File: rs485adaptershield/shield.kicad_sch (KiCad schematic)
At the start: 25 parts, among them J2 XT60, J3 RACK OUT 2mm, J4 RACK OUT 2.54mm, U2 Analog_1, U3 Analog_2, U4 ESP32-S3, U6 Digital_1, U7 Digital_2

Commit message: more work
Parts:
- removed C4, C6: 100n, Capacitor_SMD:C_0402_1005Metric, symbol Device:C
- removed J1, J5: (no value), Connector_USB:USB_C_Receptacle_GCT_USB4110, symbol Connector:USB_C_Receptacle_USB2.0_16P
- removed R14, R15, R16, R9: 5.1k, Capacitor_SMD:C_0402_1005Metric, symbol Device:R
- added C12: 100n, Capacitor_SMD:C_0402_1005Metric, symbol Device:C
- added J6: (no value), Connector_USB:USB_C_Receptacle_GCT_USB4110, symbol Connector:USB_C_Receptacle_USB2.0_16P
- added R19, R20: 5.1k, Capacitor_SMD:C_0402_1005Metric, symbol Device:R
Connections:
- net GND: now also C12.2, J6.A1 (GND), J6.A12 (GND), J6.B1 (GND), J6.B12 (GND), R19.2, R20.2
- net +3.3V: now reaches U2.4 (+3V3)
- new net: J6.A4 (VBUS), J6.A9 (VBUS), J6.B4 (VBUS), J6.B9 (VBUS)
- new net: C12.1, J6.SH (SHIELD)
- new net DC+: J6.A6 (D+), J6.B6 (D+)
- new net DC-: J6.A7 (D-), J6.B7 (D-)
- new net USB_CC1C: J6.A5 (CC1), R19.1
- new net USB_CC2C: J6.B5 (CC2), R20.1
- no-connect marks 4 -> 3
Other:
- sheet I&V Sense ports: added none; removed SCL, SDA
- note removed: "1A MAX Silkscreen"
- moved on the sheet: D1, D5, F1, J3, J4, R1, R11, U2, U4, U6, U7

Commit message: more progress
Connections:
- net VIN is gone; now on net VBATT: R1.2
- net +5V: now reaches U2.5 (+5V)
- net VBATT: now reaches U2.6 (GND)
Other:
- sheet RS485 TxRx ports: added none; removed A+, B-, DE, DI, RO, ¬RE
- note added: "Go and relabel all signals with line voltage"
- note added: "Use the dual mos package from power elec to control the usb rst and power supply enable"
- note added: "all the i/o is 5V!"
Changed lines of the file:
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@@
 	(generator_version "10.0")
 	(paper "A4")
+	(text "all the i/o is 5V!\n"
+		(exclude_from_sim no)
+		(at 130.302 105.41 0)
+		(effects
+			(font
+				(size 2.54 2.54)
+				(thickness 0.254)
+				(bold yes)
+			)
+		)
+	)
+	(text "Go and relabel all signals with line voltage\n"
+		(exclude_from_sim no)
+		(at 119.126 112.522 0)
+		(effects
+			(font
+				(size 2.54 2.54)
+				(thickness 0.254)
+				(bold yes)
+			)
+		)
+	)
 	(text "check flipping\n"
 		(exclude_from_sim no)
@@
 		)
 	)
+	(text "Use the dual mos package from power elec to control the usb rst and power supply enable"
+		(exclude_from_sim no)
+		(at 113.03 121.92 0)
+		(effects
+			(font
+				(size 2.54 2.54)
+				(thickness 0.254)
+				(bold yes)
+			)
+		)
+	)
 	(text "check flipping\n"
 		(exclude_from_sim no)
@@
 	)
 	(no_connect
-		(at 184.15 58.42)
+		(at 184.15 30.48)
 	)
 	(no_connect
-		(at 184.15 30.48)
+		(at 184.15 58.42)
 	)
 	(wire
@@
 	(wire
 		(pts
+			(xy 41.91 90.17) (xy 38.1 90.17)
+		)
+		(stroke
+			(width 0)
+			(type default)
+		)
+	)
+	(wire
+		(pts
 			(xy 105.41 41.91) (xy 107.95 41.91)
 		)
@@
 	(wire
 		(pts
+			(xy 41.91 92.71) (xy 38.1 92.71)
+		)
+		(stroke
+			(width 0)
+			(type default)
+		)
+	)
+	(wire
+		(pts
 			(xy 73.66 41.91) (xy 81.28 41.91)
 		)
@@
 		)
 	)
-	(label "B-"
-		(at 228.6 114.3 0)
-		(effects
-			(font
-				(size 1.27 1.27)
-			)
-			(justify left bottom)
-		)
-	)
 	(label "A+"
 		(at 228.6 35.56 270)
@@
 		)
 	)
-	(label "¬RE"
-		(at 213.36 111.76 180)
-		(effects
-			(font
-				(size 1.27 1.27)
-			)
-			(justify right bottom)
-		)
-	)
 	(label "DC-"
 		(at 186.69 45.72 0)
@@
 		)
 	)
-	(label "DI"
-		(at 213.36 116.84 180)
-		(effects
-			(font
-				(size 1.27 1.27)
-			)
-			(justify right bottom)
-		)
-	)
-	(label "A+"
-		(at 228.6 111.76 0)
-		(effects
-			(font
-				(size 1.27 1.27)
-			)
-			(justify left bottom)
-		)
-	)
-	(label "DE"
-		(at 213.36 114.3 180)
-		(effects
-			(font
-				(size 1.27 1.27)
-			)
-			(justify right bottom)
-		)
-	)
 	(label "AUX2"
 		(at 236.22 58.42 270)
@@
 		)
 	)
-	(label "RO"
-		(at 213.36 109.22 180)
-		(effects
-			(font
-				(size 1.27 1.27)
-			)
-			(justify right bottom)
-		)
-	)
 	(symbol
 		(lib_id "power:+5V")
@@
 	)
 	(symbol
+		(lib_id "power:+12V")
+		(at 41.91 92.71 270)
+		(mirror x)
+		(unit 1)
+		(body_style 1)
+		(exclude_from_sim no)
+		(in_bom yes)
+		(on_board yes)
+		(in_pos_files yes)
+		(dnp no)
+		(property "Reference" "#PWR010"
+			(at 38.1 92.71 0)
+			(hide yes)
+			(show_name no)
+			(do_not_autoplace no)
+			(effects
+				(font
+					(size 1.27 1.27)
+				)
+			)
+		)
+		(property "Value" "VBATT"
+			(at 51.562 92.71 90)
+			(show_name no)
+			(do_not_autoplace no)
+			(effects
+				(font
+					(size 1.27 1.27)
+				)
+				(justify right)
+			)
+		)
+		(property "Footprint" ""
+			(at 41.91 92.71 0)
+			(hide yes)
+			(show_name no)
+			(do_not_autoplace no)
+			(effects
+				(font
+					(size 1.27 1.27)
+				)
+			)
+		)
+		(property "Datasheet" ""
+			(at 41.91 92.71 0)
+			(hide yes)
+			(show_name no)
+			(do_not_autoplace no)
+			(effects
+				(font
+					(size 1.27 1.27)
+				)
+			)
+		)
+		(property "Description" "Power symbol creates a global label with name \"+12V\""
+			(at 41.91 92.71 0)
+			(hide yes)
+			(show_name no)
+			(do_not_autoplace no)
+			(effects
+				(font
+					(size 1.27 1.27)
+				)
+			)
+		)
+		(pin "1"
+		)
+		(instances
+			(project "shield"
+				(path "/4deaa014-311e-404e-963e-ca894f6a7656"
+					(reference "#PWR010")
+					(unit 1)
+				)
+			)
+		)
+	)
+	(symbol
 		(lib_id "Device:C")
 		(at 154.94 72.39 270)
@@
 	)
 	(symbol
+		(lib_id "power:+3.3V")
+		(at 41.91 90.17 270)
+		(unit 1)
+		(body_style 1)
+		(exclude_from_sim no)
+		(in_bom yes)
+		(on_board yes)
+		(in_pos_files yes)
+		(dnp no)
+		(fields_autoplaced yes)
+		(property "Reference" "#PWR036"
+			(at 38.1 90.17 0)
+			(hide yes)
+			(show_name no)
+			(do_not_autoplace no)
+			(effects
+				(font
+					(size 1.27 1.27)
+				)
+			)
+		)
+		(property "Value" "+5V"
+			(at 45.72 90.1699 90)
+			(show_name no)
+			(do_not_autoplace no)
+			(effects
+				(font
+					(size 1.27 1.27)
+				)
+				(justify left)
+			)
+		)
+		(property "Footprint" ""
+			(at 41.91 90.17 0)
+			(hide yes)
+			(show_name no)
+			(do_not_autoplace no)
+			(effects
+				(font
+					(size 1.27 1.27)
+				)
+			)
+		)
+		(property "Datasheet" ""
+			(at 41.91 90.17 0)
+			(hide yes)
+			(show_name no)
+			(do_not_autoplace no)
+			(effects
+				(font
+					(size 1.27 1.27)
+				)
+			)
+		)
+		(property "Description" "Power symbol creates a global label with name \"+3.3V\""
+			(at 41.91 90.17 0)
+			(hide yes)
+			(show_name no)
+			(do_not_autoplace no)
+			(effects
+				(font
+					(size 1.27 1.27)
+				)
+			)
+		)
+		(pin "1"
+		)
+		(instances
+			(project "shield"
+				(path "/4deaa014-311e-404e-963e-ca894f6a7656"
+					(reference "#PWR036")
+					(unit 1)
+				)
+			)
+		)
+	)
+	(symbol
 		(lib_id "power:GND")
 		(at 81.28 69.85 0)
@@
 			)
 		)
-		(property "Value" "VIN"
+		(property "Value" "VBATT"
 			(at 106.426 32.766 0)
 			(show_name no)
@@
 	)
 	(sheet
-		(at 26.67 53.34)
+		(at 58.42 85.09)
 		(size 15.24 11.43)
 		(exclude_from_sim no)
@@
 		)
 		(property "Sheetname" "Power Supply"
-			(at 26.67 52.6284 0)
+			(at 58.42 84.3784 0)
 			(show_name no)
 			(do_not_autoplace no)
@@
 		)
 		(property "Sheetfile" "psu.kicad_sch"
-			(at 26.67 65.3546 0)
+			(at 58.42 97.1046 0)
 			(show_name no)
 			(do_not_autoplace no)
@@
 	)
 	(sheet
-		(at 213.36 106.68)
-		(size 15.24 12.7)
+		(at 209.55 90.17)
+		(size 15.24 11.43)
 		(exclude_from_sim no)
 		(in_bom yes)
@@
 		)
 		(property "Sheetname" "RS485 TxRx"
-			(at 213.36 105.9684 0)
+			(at 209.55 89.4584 0)
 			(show_name no)
 			(do_not_autoplace no)
@@
 		)
 		(property "Sheetfile" "rs485.kicad_sch"
-			(at 213.36 119.9646 0)
+			(at 209.55 102.1846 0)
 			(show_name no)
 			(do_not_autoplace no)
@@
 			)
 		)
-		(pin "B-" output
-			(at 228.6 114.3 0)
-			(effects
-				(font
-					(size 1.27 1.27)
-				)
-				(justify right)
-			)
-		)
-		(pin "A+" output
-			(at 228.6 111.76 0)
-			(effects
-				(font
-					(size 1.27 1.27)
-				)
-				(justify right)
-			)
-		)
-		(pin "RO" input
-			(at 213.36 109.22 180)
-			(effects
-				(font
-					(size 1.27 1.27)
-				)
-				(justify left)
-			)
-		)
-		(pin "DI" input
-			(at 213.36 116.84 180)
-			(effects
-				(font
-					(size 1.27 1.27)
-				)
-				(justify left)
-			)
-		)
-		(pin "¬RE" input
-			(at 213.36 111.76 180)
-			(effects
-				(font
-					(size 1.27 1.27)
-				)
-				(justify left)
-			)
-		)
-		(pin "DE" input
-			(at 213.36 114.3 180)
-			(effects
-				(font
-					(size 1.27 1.27)
-				)
-				(justify left)
-			)
-		)
 		(instances
 			(project "shield"
@@
 	)
 	(sheet
-		(at 181.61 76.2)
+		(at 162.56 132.08)
 		(size 25.4 16.51)
 		(exclude_from_sim no)
@@
 		)
 		(property "Sheetname" "USB"
-			(at 181.61 75.4884 0)
+			(at 162.56 131.3684 0)
 			(show_name no)
 			(do_not_autoplace no)
@@
 		)
 		(property "Sheetfile" "usb.kicad_sch"
-			(at 181.61 93.2946 0)
+			(at 162.56 149.1746 0)
 			(show_name no)
 			(do_not_autoplace no)

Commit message: reminder
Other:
- note added: "diagram reminder"
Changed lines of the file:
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@@
+		)
+	)
+	(text "diagram reminder"
+		(exclude_from_sim no)
+		(at 71.12 142.494 0)
+		(effects
+			(font
+				(size 1.27 1.27)
+			)
 		)
 	)

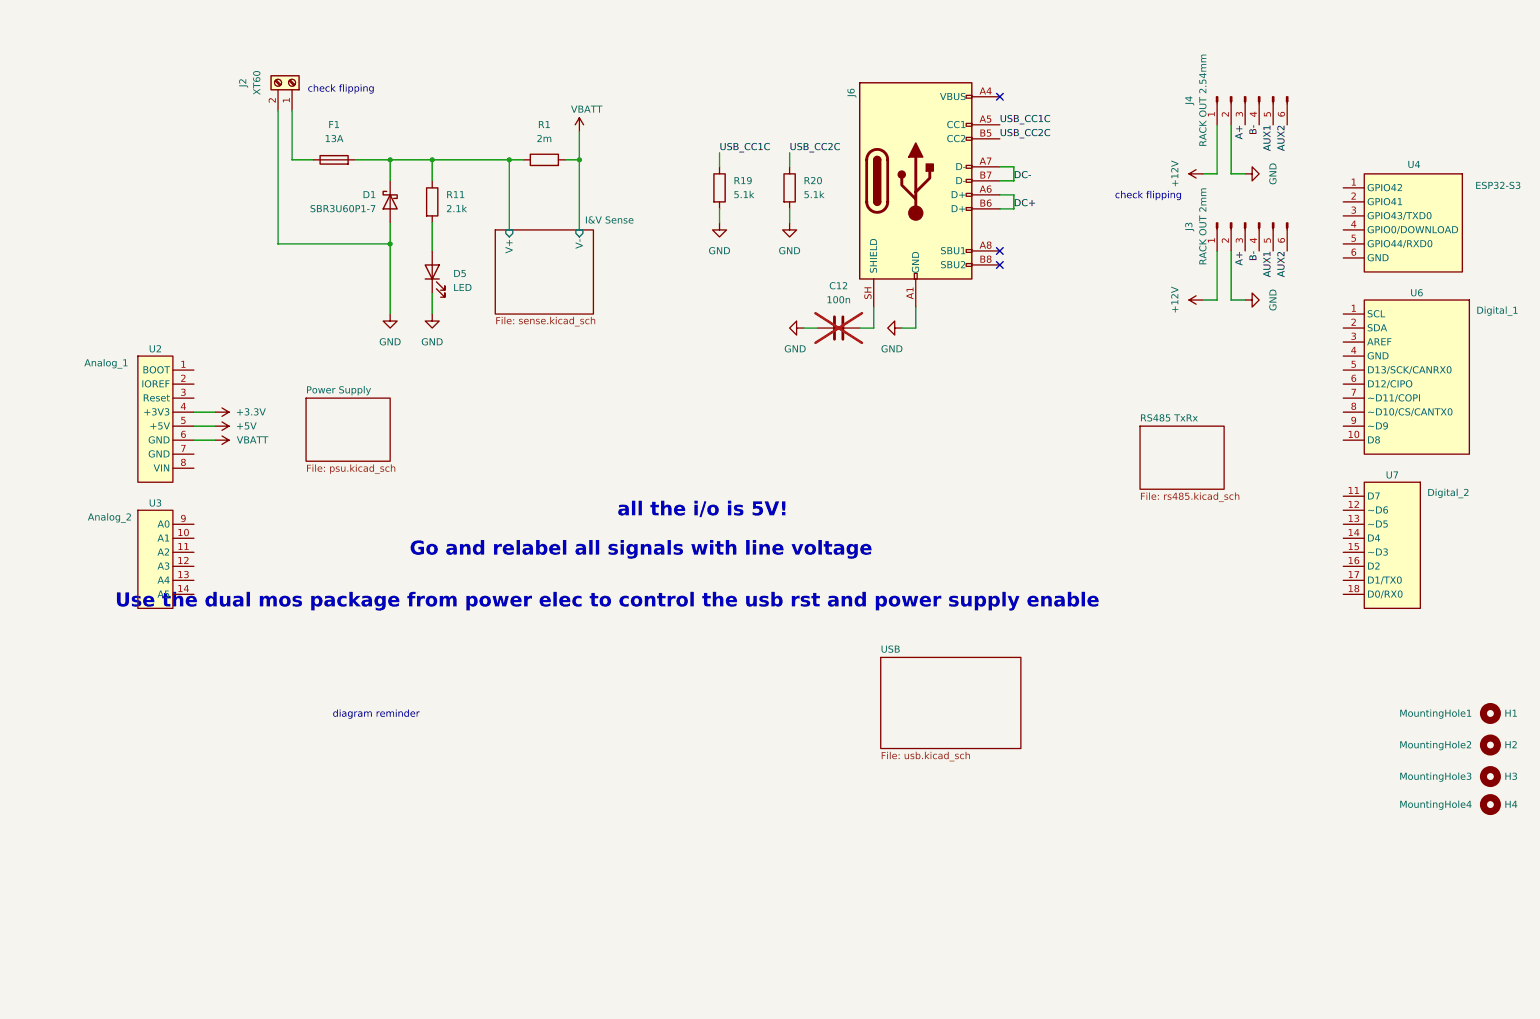
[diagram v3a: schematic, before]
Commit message: schematic mostly finished w/o footprints
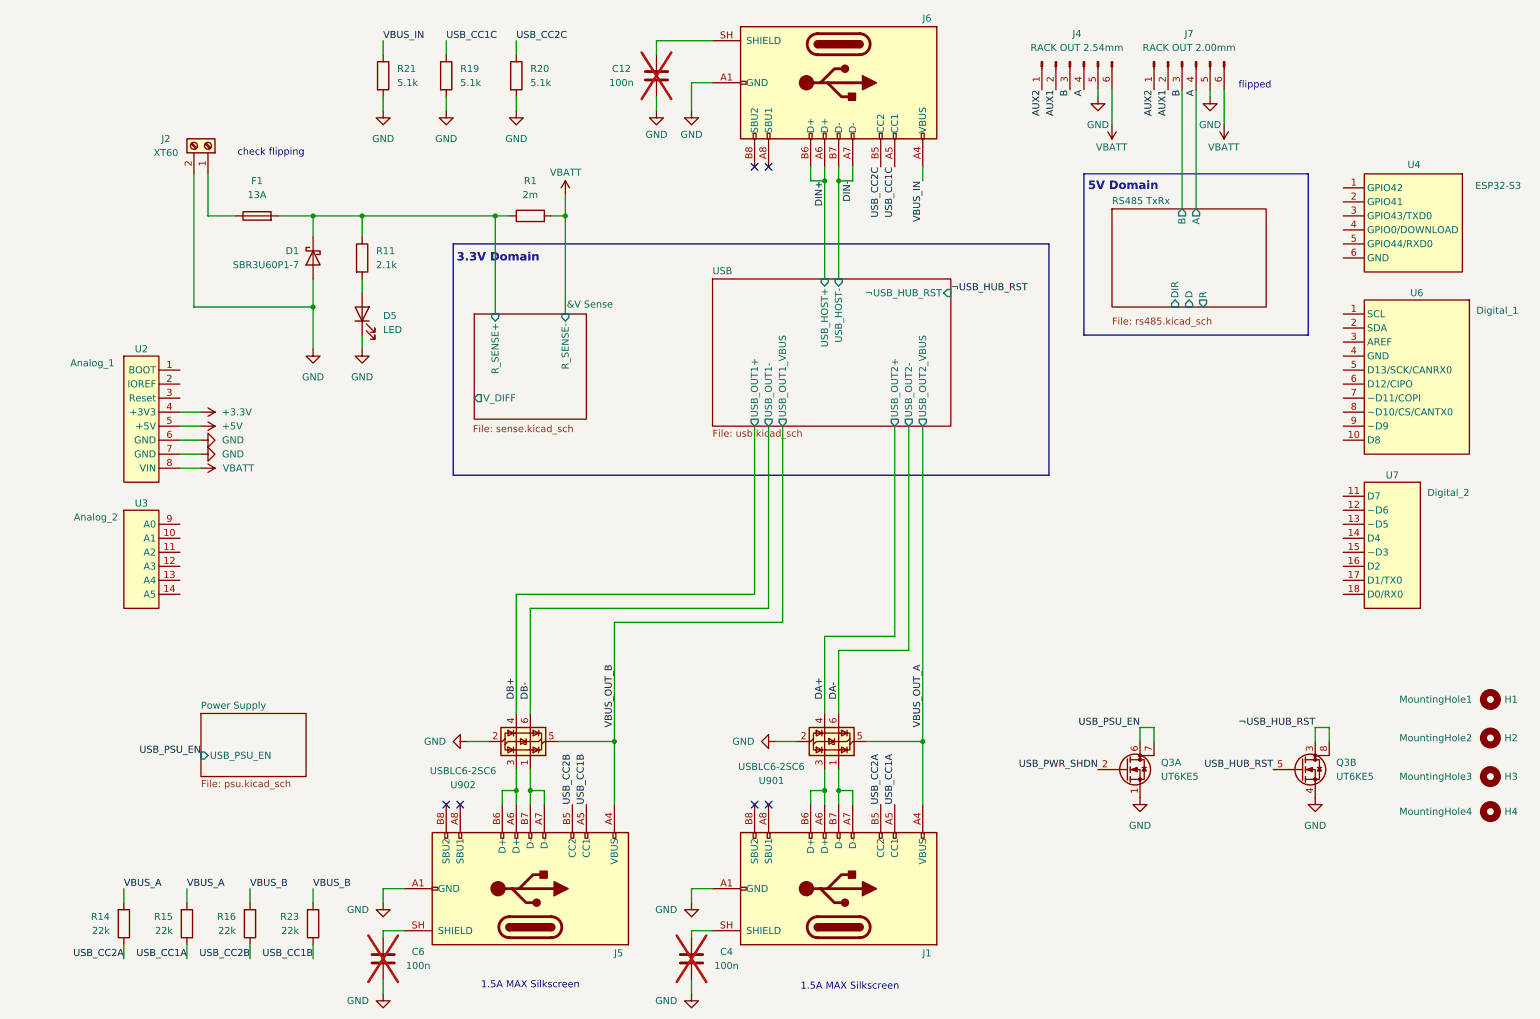
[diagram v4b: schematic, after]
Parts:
- removed J3: RACK OUT 2mm, Connector_PinHeader_2.00mm:PinHeader_1x06_P2.00mm_Vertical, symbol Connector:Conn_01x06_Pin
- added C4, C6: 100n, Capacitor_SMD:C_0402_1005Metric, symbol Device:C
- added J1, J5: (no value), Connector_USB:USB_C_Receptacle_GCT_USB4110, symbol Connector:USB_C_Receptacle_USB2.0_16P
- added J7: RACK OUT 2.00mm, Connector_PinHeader_2.54mm:PinHeader_1x06_P2.00mm_Vertical, symbol Connector:Conn_01x06_Pin
- added Q3: UT6KE5, UT6:UT6KE5TCR, symbol UT6:UT6
- added R14, R15, R16, R23: 22k, Capacitor_SMD:C_0402_1005Metric, symbol Device:R
- added R21: 5.1k, Capacitor_SMD:C_0402_1005Metric, symbol Device:R
- added U901, U902: USBLC6-2SC6, Package_TO_SOT_SMD:SOT-23-6, symbol Power_Protection:USBLC6-2SC6
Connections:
- net +12V is gone; now on net AUX2: J4.1 (Pin_1)
- net AUX1: now also J4.2 (Pin_2), J7.2 (Pin_2); no longer J4.5 (Pin_5)
- net AUX2: now also J7.1 (Pin_1); no longer J4.6 (Pin_6)
- net GND: now also J4.5 (Pin_5), U2.6 (GND), U2.7 (GND), C4.2, C6.2, J1.A1 (GND), J1.A12 (GND), J1.B1 (GND), J1.B12 (GND), J5.A1 (GND), J5.A12 (GND), J5.B1 (GND), J5.B12 (GND), J7.5 (Pin_5), Q3.1 (S), Q3.4 (S), R21.2, U901.2 (GND), U902.2 (GND); no longer J4.2 (Pin_2)
- net VBATT: now also J4.6 (Pin_6), U2.8 (VIN), J7.6 (Pin_6); no longer U2.6 (GND)
- net VBUS_IN: now reaches J6.A4 (VBUS), J6.A9 (VBUS), J6.B4 (VBUS), J6.B9 (VBUS)
- net VBUS_IN: now also R21.1
- net A+ renamed B
- net B: now also J7.3 (Pin_3)
- net B- renamed A
- net A: now also J7.4 (Pin_4)
- net DC+ renamed DIN+
- net DC- renamed DIN-
- net I&V Sense/V+ renamed I&V Sense/R_SENSE+
- new net: J5.A6 (D+), J5.B6 (D+), U902.3 (I/O2)
- new net: J5.A7 (D-), J5.B7 (D-), U902.1 (I/O1)
- new net: C6.1, J5.SH (SHIELD)
- new net: J1.A7 (D-), J1.B7 (D-), U901.1 (I/O1)
- new net: J1.A6 (D+), J1.B6 (D+), U901.3 (I/O2)
- new net: C4.1, J1.SH (SHIELD)
- new net DA+: U901.4 (I/O2)
- new net DA-: U901.6 (I/O1)
- new net DB+: U902.4 (I/O2)
- new net DB-: U902.6 (I/O1)
- new net USB_CC1A: J1.A5 (CC1), R15.1
- new net USB_CC1B: J5.A5 (CC1), R23.1
- new net USB_CC2A: J1.B5 (CC2), R14.1
- new net USB_CC2B: J5.B5 (CC2), R16.1
- new net USB_HUB_RST: Q3.5 (G)
- new net USB_PSU_EN: Q3.6 (D), Q3.7 (D)
- new net USB_PWR_SHDN: Q3.2 (G)
- new net VBUS_A: R14.2, R15.2
- new net VBUS_B: R16.2, R23.2
- new net VBUS_OUT_A: J1.A4 (VBUS), J1.A9 (VBUS), J1.B4 (VBUS), J1.B9 (VBUS), U901.5 (VBUS)
- new net VBUS_OUT_B: J5.A4 (VBUS), J5.A9 (VBUS), J5.B4 (VBUS), J5.B9 (VBUS), U902.5 (VBUS)
- new net ¬USB_HUB_RST: Q3.3 (D), Q3.8 (D)
- no-connect marks 3 -> 6
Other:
- sheet I&V Sense ports: added R_SENSE+, R_SENSE-, V_DIFF; removed V+, V-
- sheet Power Supply ports: added USB_PSU_EN; removed none
- sheet RS485 TxRx ports: added A, B, D, DIR, R; removed none
- sheet USB ports: added USB_HOST+, USB_HOST-, USB_OUT1+, USB_OUT1-, USB_OUT1_VBUS, USB_OUT2+, USB_OUT2-, USB_OUT2_VBUS, ¬USB_HUB_RST; removed none
- note added: "1.5A MAX Silkscreen"
- note added: "3.3V Domain"
- note added: "5V Domain"
- note added: "flipped"
- note removed: "Go and relabel all signals with line voltage"
- note removed: "Use the dual mos package from power elec to control the usb rst and power supply enable"
- note removed: "all the i/o is 5V!"
- note removed: "diagram reminder"
- moved on the sheet: D1, D5, F1, H1, H2, H4, J2, J4, R1, R11, U2, U3

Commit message: usb stackup problems
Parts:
- removed C4, C6: 100n, Capacitor_SMD:C_0402_1005Metric, symbol Device:C
- removed H1: MountingHole1, ArduinoMountingHoles:Arduino_MountingHole, symbol Mechanical_Arduino:MountingHole_Arduino
- removed H3: MountingHole3, ArduinoMountingHoles:Arduino_MountingHole, symbol Mechanical_Arduino:MountingHole_Arduino
- removed J4: RACK OUT 2.54mm, Connector_PinHeader_2.54mm:PinHeader_1x06_P2.54mm_Vertical, symbol Connector:Conn_01x06_Pin
- removed U4: ESP32-S3, ArduinoPinSockets:Arduino_PinSocket_2x03_P2.54mm_Vertical, symbol Connector_Arduino:Arduino_Header_ESP32-S3
- added C32, C40: 22u, Capacitor_SMD:C_1210_3225Metric, symbol Device:C
- added C36, C37: 100n, Capacitor_SMD:C_0402_1005Metric, symbol Device:C
- added F2: 13A, Fuse:Fuse_1812_4532Metric, symbol Device:Fuse
- added R30, R31, R38: 1M, Resistor_SMD:R_0402_1005Metric, symbol Device:R
- added U903: USBLC6-2SC6, Package_TO_SOT_SMD:SOT-23-6, symbol Power_Protection:USBLC6-2SC6
- C12: now fitted
- D5: footprint LED_SMD:LED_0805_2012Metric -> LED_SMD:LED_0603_1608Metric
- J7: footprint Connector_PinHeader_2.54mm:PinHeader_1x06_P2.00mm_Vertical -> Connector_PinHeader_2.00mm:PinHeader_1x06_P2.00mm_Vertical
- Q3: footprint UT6:UT6KE5TCR -> IMPORTED:UT6KE5TCR
- R1, R11: footprint Resistor_SMD:R_0805_2012Metric -> Resistor_SMD:R_0603_1608Metric
- R14, R15, R16, R19, R20, R21, R23: footprint Capacitor_SMD:C_0402_1005Metric -> Resistor_SMD:R_0402_1005Metric
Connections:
- net DIN+: now also U903.4 (I/O2)
- net DIN-: now also U903.6 (I/O1)
- net GND: now also C32.2, C36.2, C37.2, C40.2, R30.1, R31.1, R38.1, U903.2 (GND)
- net RS485 TxRx/D: now also U7.17 (D1/TX0)
- net RS485 TxRx/R: now also U7.18 (D0/RX0)
- net USB_PSU_EN: now also U7.11 (D7)
- net VBATT: now also F2.1; no longer J7.6 (Pin_6)
- net VBUS_IN: now also U903.5 (VBUS)
- net ¬USB_HUB_RST: now also U7.12 (~D6)
- net at J5.SH (SHIELD): now also C37.1, R30.2
- net at C12.1, J6.SH (SHIELD): now also R38.2
- net RS485 TxRx/¬RE: now reaches U7.16 (D2)
- net at J1.SH (SHIELD): now also C36.1, R31.2
- net T_SENSE: now reaches U3.10 (A1)
- net I_SENSE: now reaches U3.9 (A0)
- new net: C32.1, C40.1, F2.2, J7.6 (Pin_6)
- new net USB/USB_HOST+: U903.3 (I/O2)
- new net USB/USB_HOST-: U903.1 (I/O1)
- no-connect marks 6 -> 26
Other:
- sheet I&V Sense renamed Current and Temp Sense
- sheet Current and Temp Sense ports: added I_SENSE, T_SENSE; removed V_DIFF
- sheet RS485 TxRx ports: added ¬RE; removed DIR
- moved on the sheet: H2, H4, J5, J7, Q3A, Q3B, R14, R15, R16, R23, U902

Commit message: netclass bullshit
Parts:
- removed U903: USBLC6-2SC6, Package_TO_SOT_SMD:SOT-23-6, symbol Power_Protection:USBLC6-2SC6
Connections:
- net Current and Temp Sense/R_SENSE+: no longer D1.1 (K)
- net VBATT: now also D1.1 (K)
- net DCONN_2+: now reaches J5.A6 (D+), J5.B6 (D+), U902.3 (I/O2)
- net DCONN_2-: now reaches J5.A7 (D-), J5.B7 (D-), U902.1 (I/O1)
- net DCONN_1-: now reaches J1.A7 (D-), J1.B7 (D-), U901.1 (I/O1)
- net DCONN_1+: now reaches J1.A6 (D+), J1.B6 (D+), U901.3 (I/O2)
- net DIN+ renamed DI+
- net DIN- renamed DI-
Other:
- moved on the sheet: D1, D5, F1, J2, R1, R11

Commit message: pushes
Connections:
- net Current and Temp Sense/R_SENSE+: no longer R11.1
- net USB_HUB_RST: now also U7.11 (D7)
- net USB_PSU_EN: no longer U7.11 (D7)
- net USB_PWR_SHDN: now also U7.12 (~D6)
- net VBATT: now also C32.1, C40.1, R11.1
- net ¬USB_HUB_RST: no longer U7.12 (~D6)
- net at F2.2, J7.6 (Pin_6): no longer C32.1, C40.1
- net DA+ renamed DA_P
- net DA- renamed DA_N
- net DB+ renamed DB _P
- net DB- renamed DB_N
- net DCONN_1+: no longer names the net of J1.A6 (D+), J1.B6 (D+), U901.3 (I/O2)
- net DCONN_1-: no longer names the net of J1.A7 (D-), J1.B7 (D-), U901.1 (I/O1)
- net DCONN_2+: no longer names the net of J5.A6 (D+), J5.B6 (D+), U902.3 (I/O2)
- net DCONN_2-: no longer names the net of J5.A7 (D-), J5.B7 (D-), U902.1 (I/O1)
- net DI+ renamed DI_P
- net DI- renamed DI_N
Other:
- moved on the sheet: C32, C40, F1, F2, J2
